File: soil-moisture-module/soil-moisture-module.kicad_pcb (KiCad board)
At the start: 2 copper layers, 116.8 x 27.9 mm, 26 parts, among them J1 MODULE_HEADER, J2 CONN_02X03, J3 CONN_02X03, J4 CONN_02X03, J5 CONN_02X03, Q1 2N7002, Q2 2N7002, U1 ATTINY24-SS

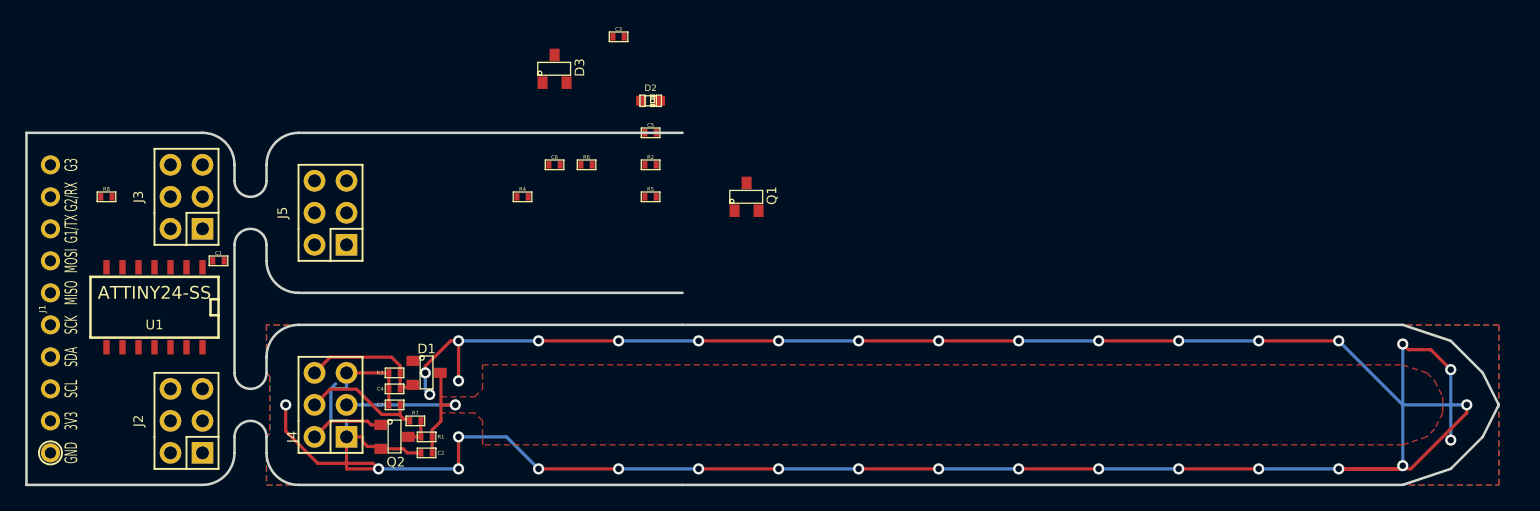
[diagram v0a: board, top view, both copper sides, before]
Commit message: pinswap on PD diodes, second probe done. capacitances are approximate. ready to build, but next up is an experiment to maximize "edge" capacitance (at the expense of "substrate" capacitance).
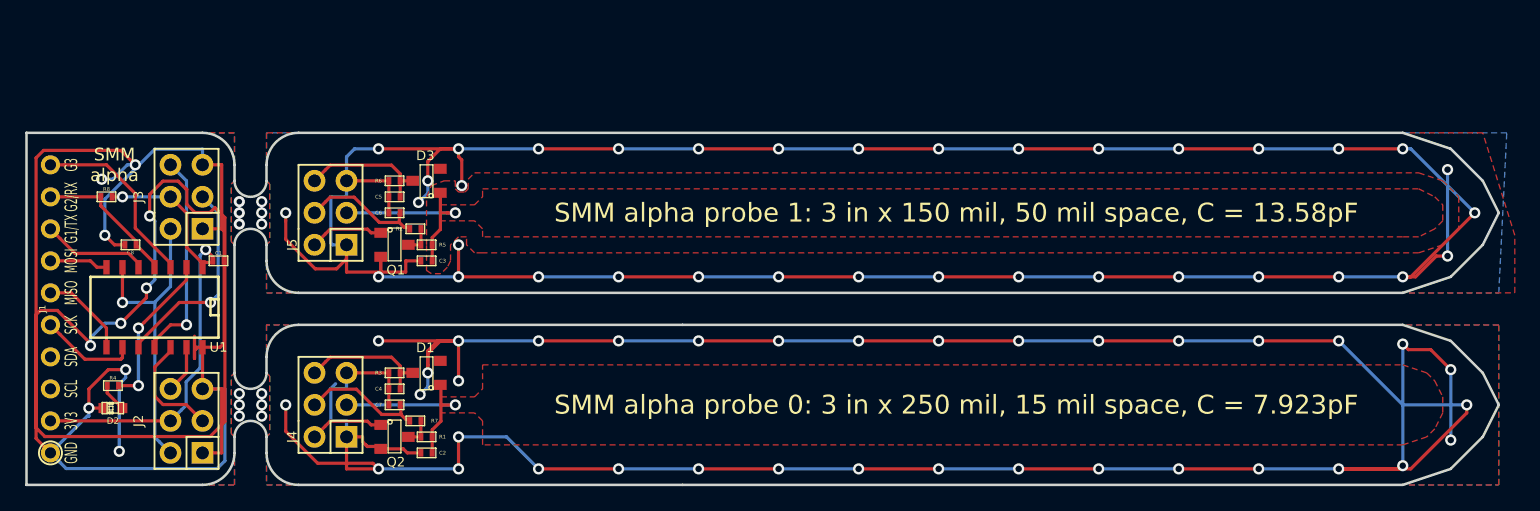
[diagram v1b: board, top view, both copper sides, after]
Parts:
- added C8: 100nF, parts:SMD-0402, F.Cu at (109.9, 108.0)
- moved D2 49.1 mm to (108.5, 120.9), turned to 180 degrees
- moved R4 35.8 mm to (108.5, 119.1)
- moved Q1 28.2 mm to (130.8, 108.0), turned to 270 degrees
- moved C3 23.4 mm to (133.3, 109.2), turned to 180 degrees
- moved C5 20.9 mm to (130.8, 104.1), turned to 180 degrees
- moved R2 19.3 mm to (132.5, 106.7), turned to 180 degrees
- moved R5 18.2 mm to (133.3, 108.0), turned to 180 degrees
- moved R6 15.3 mm to (130.8, 102.9)
- moved D3 13.5 mm to (133.3, 102.9), turned to 90 degrees
- moved C6 13.3 mm to (130.8, 105.4), turned to 180 degrees
- turned D1 to 90 degrees
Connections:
- D1 pad 1: Net-(D1-Pad1) -> /LPF0_OUT
- D1 pad 2: /PD0_OUT -> Net-(D1-Pad2)
- D1 pad 3: /LPF0_OUT -> /PD0_OUT
- D3 pad 1: Net-(D3-Pad1) -> /LPF1_OUT
- D3 pad 2: /PD1_OUT -> Net-(D3-Pad2)
- D3 pad 3: /LPF1_OUT -> /PD1_OUT
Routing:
- net /GND1: track 0.00 -> 240.6 mm, vias 0 -> 36
- net GND: track 0.00 -> 195.0 mm, vias 0 -> 10
- net +3.3V: track 0.00 -> 37.9 mm, vias 0 -> 2
- net /WAVE_OUT: track 0.00 -> 24.2 mm, vias 0 -> 1
- net /PD1_IN: track 0.00 -> 16.8 mm, vias 0 -> 1
- net /LED: track 0.00 -> 16.6 mm, vias 0 -> 2
- net /LPF1_IN: track 0.00 -> 16.5 mm, vias 0 -> 1
- net /LPF1_OUT: track 0.00 -> 15.5 mm, vias 0 -> 1
- net /IRQ: track 0.00 -> 14.7 mm
- net /GND0: track 245.3 -> 256.7 mm, vias 35 -> 36
- net /~RESET: track 0.00 -> 11.3 mm
- net /PD1_OUT: track 0.00 -> 10.4 mm
- net /3.3V_PROBE_1: track 0.00 -> 9.90 mm
- net /LPF0_IN: track 0.00 -> 9.00 mm
- net /CS: track 0.00 -> 8.43 mm
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- added copper zone on B.Cu, net /GND1
- added copper zone on F.Cu, net /GND1
- added copper zone on F.Cu, net /LPF1_OUT
- added copper zone on B.Cu, net GND
- added copper zone on F.Cu, net GND
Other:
- outline, holes or cut-outs redrawn
- net class Default: clearance 0.254 -> 0.2032
- rule trace_clearance: 0.254 -> 0.2032
- board text added: "SMM alpha"
- board text added: "SMM alpha probe 0: 3 in x 250 mil, 15 mil space, C = 7.923pF"
- board text added: "SMM alpha probe 1: 3 in x 150 mil, 50 mil space, C = 13.58pF"

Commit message: derp... the silk was swapped
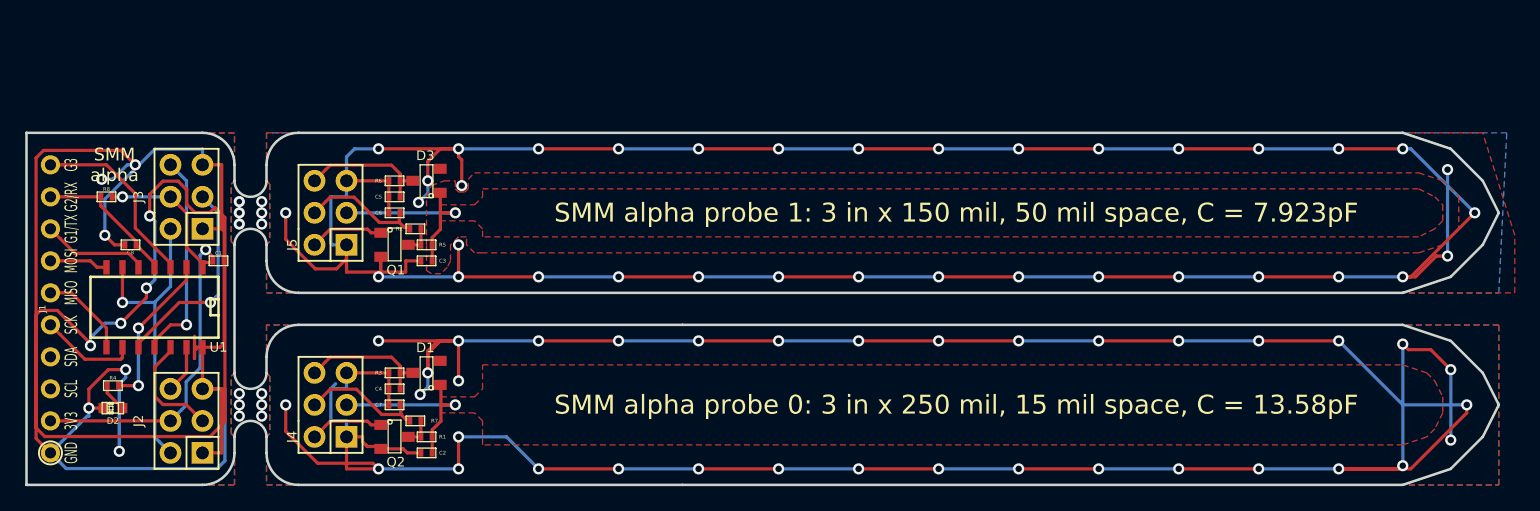
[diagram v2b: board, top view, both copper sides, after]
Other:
- board text added: "SMM alpha probe 0: 3 in x 250 mil, 15 mil space, C = 13.58pF"
- board text added: "SMM alpha probe 1: 3 in x 150 mil, 50 mil space, C = 7.923pF"
- board text removed: "SMM alpha probe 0: 3 in x 250 mil, 15 mil space, C = 7.923pF"
- board text removed: "SMM alpha probe 1: 3 in x 150 mil, 50 mil space, C = 13.58pF"
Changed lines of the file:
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@@
     )
   )
-  (gr_text "SMM alpha probe 0: 3 in x 250 mil, 15 mil space, C = 7.923pF" (at 175.387 120.65) (layer F.SilkS)
+  (gr_text "SMM alpha probe 0: 3 in x 250 mil, 15 mil space, C = 13.58pF" (at 175.387 120.65) (layer F.SilkS)
     (effects (font (size 1.5 1.5) (thickness 0.3)))
   )
-  (gr_text "SMM alpha probe 1: 3 in x 150 mil, 50 mil space, C = 13.58pF" (at 175.387 105.41) (layer F.SilkS)
+  (gr_text "SMM alpha probe 1: 3 in x 150 mil, 50 mil space, C = 7.923pF" (at 175.387 105.41) (layer F.SilkS)
     (effects (font (size 1.5 1.5) (thickness 0.3)))
   )

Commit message: high-performance probe? we hope!
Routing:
- net /GND1: track 240.6 -> 229.6 mm
- net /LPF1_OUT: track 15.5 -> 16.8 mm
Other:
- board text added: "SMM alpha probe 0: 3 in x 250 mil, 15 mil space C_b_FR4 = 12.85pF C_p_FR4 = 0.7287pF C_p_H2O = 13.859pF"
- board text added: "SMM alpha probe 1: 20 mil x 170 mil 52-comb, 10 mil space C_b_FR4 = 6.903pF C_p_FR4 = 6.477pF C_p_H2O = 118.7pF"
- board text removed: "SMM alpha probe 0: 3 in x 250 mil, 15 mil space, C = 13.58pF"
- board text removed: "SMM alpha probe 1: 3 in x 150 mil, 50 mil space, C = 7.923pF"

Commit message: so many polygons... super high performance probe? probably.
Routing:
- net /GND0: track 256.7 -> 122.2 mm, vias 36 -> 17
- net /LPF1_OUT: track 16.8 -> 115.8 mm, vias 1 -> 4
- net /GND1: track 229.6 -> 231.2 mm
- added copper zone on B.Cu, net /LPF1_OUT
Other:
- board text added: "SMM alpha probe 0: 3 in x 250/180 mil, 15/50 mil space C_b_FR4 = 6.425pF C_p_FR4 = 0.7287pF C_p_H2O = 13.859pF"
- board text added: "SMM alpha probe 1: 20 mil x 170 mil 52-comb, 10 mil space C_b_FR4 = 3.4515pF C_p_FR4 = 9.7155pF C_p_H2O = 178.05pF"
- board text removed: "SMM alpha probe 0: 3 in x 250 mil, 15 mil space C_b_FR4 = 12.85pF C_p_FR4 = 0.7287pF C_p_H2O = 13.859pF"
- board text removed: "SMM alpha probe 1: 20 mil x 170 mil 52-comb, 10 mil space C_b_FR4 = 6.903pF C_p_FR4 = 6.477pF C_p_H2O = 118.7pF"

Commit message: gerbers for alpha build
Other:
- rule pad_to_mask_clearance: 0 -> 0.0762
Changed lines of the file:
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@@
     (links 63)
     (no_connects 0)
-    (area 92.024287 86.050001 424.624501 265.557001)
+    (area 92.024287 86.050001 226.745715 137.828001)
     (thickness 1.6)
     (drawings 93)
@@
     (pad_size 1.5 1.5)
     (pad_drill 0.6)
-    (pad_to_mask_clearance 0)
+    (pad_to_mask_clearance 0.0762)
     (aux_axis_origin 101.6 127)
     (grid_origin 101.6 127)
     (visible_elements FFFFFF7F)
     (pcbplotparams
-      (layerselection 0x00030_80000001)
+      (layerselection 0x010e0_80000001)
       (usegerberextensions false)
       (excludeedgelayer true)
@@
       (plotinvisibletext false)
       (padsonsilk false)
-      (subtractmaskfromsilk false)
+      (subtractmaskfromsilk true)
       (outputformat 1)
       (mirror false)
-      (drillshape 1)
+      (drillshape 0)
       (scaleselection 1)
-      (outputdirectory ""))
+      (outputdirectory gerbers-soil-moisture/))
   )
   (net 0 "")
@@
     (at 116.84 109.22)
     (attr smd)
-    (fp_text reference C1 (at 0 -0.6096) (layer F.SilkS)
+    (fp_text reference C1 (at 0 -0.635) (layer F.SilkS)
       (effects (font (size 0.3 0.3) (thickness 0.05)))
     )
@@
     (at 108.458 119.126)
     (attr smd)
-    (fp_text reference R4 (at 0 -0.6096) (layer F.SilkS)
+    (fp_text reference R4 (at -1.27 0) (layer F.SilkS)
       (effects (font (size 0.3 0.3) (thickness 0.05)))
     )
@@
     (at 107.95 104.14)
     (attr smd)
-    (fp_text reference R8 (at 0 -0.6096) (layer F.SilkS)
+    (fp_text reference R8 (at -1.27 0) (layer F.SilkS)
       (effects (font (size 0.3 0.3) (thickness 0.05)))
     )
@@
     (at 109.855 107.95 180)
     (attr smd)
-    (fp_text reference C8 (at 0 -0.6096 180) (layer F.SilkS)
-      (effects (font (size 0.3 0.3) (thickness 0.05)))
-    )
+    (fp_text reference C8 (at 1.27 0 180) (layer F.SilkS)
+      (effects (font (size 0.3 0.3) (thickness 0.05)))
+    )
